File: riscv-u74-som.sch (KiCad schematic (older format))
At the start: 0 parts

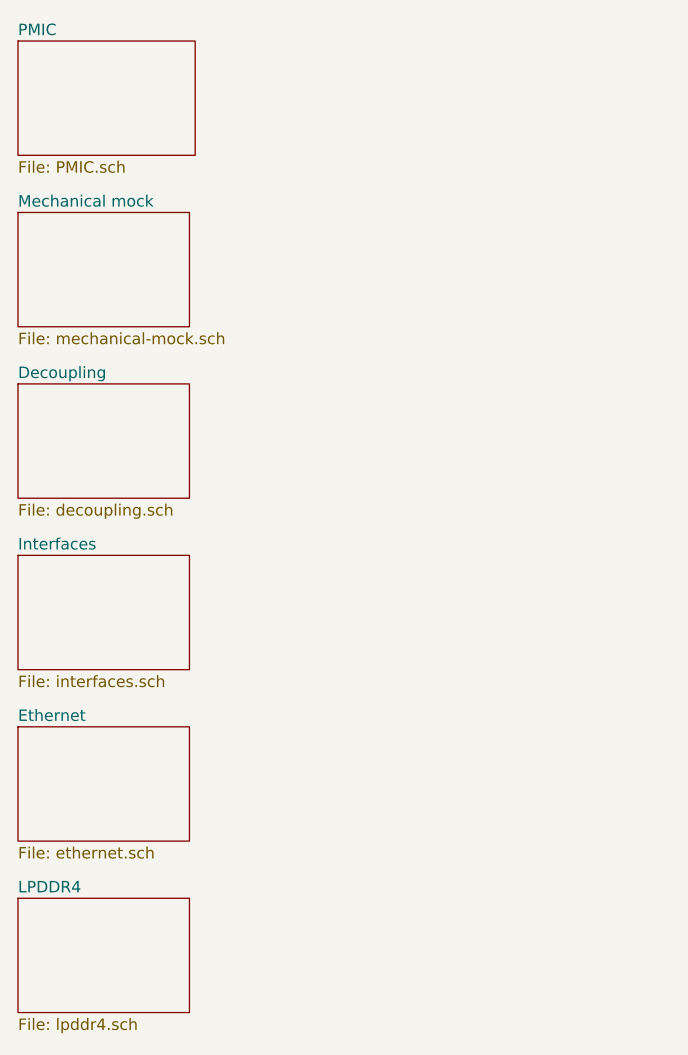
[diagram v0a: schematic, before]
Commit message: Added processor and B2B sheets
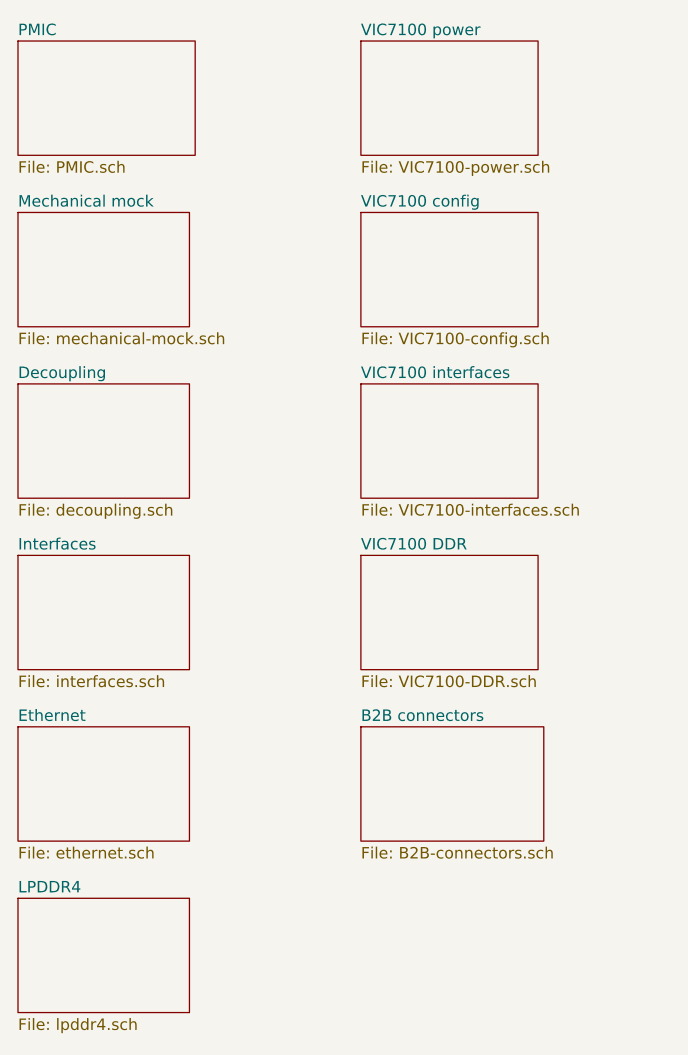
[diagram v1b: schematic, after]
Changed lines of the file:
@@
 $Descr A4 11693 8268
 encoding utf-8
-Sheet 1 7
+Sheet 1 12
 Title ""
 Date ""
@@
 F1 "lpddr4.sch" 50
 $EndSheet
+$Sheet
+S 3000 1000 775  500
+U 60805C73
+F0 "VIC7100 power" 50
+F1 "VIC7100-power.sch" 50
+$EndSheet
+$Sheet
+S 3000 1750 775  500
+U 60805CC6
+F0 "VIC7100 config" 50
+F1 "VIC7100-config.sch" 50
+$EndSheet
+$Sheet
+S 3000 2500 775  500
+U 60805CEC
+F0 "VIC7100 interfaces" 50
+F1 "VIC7100-interfaces.sch" 50
+$EndSheet
+$Sheet
+S 3000 3250 775  500
+U 613A40EE
+F0 "VIC7100 DDR" 50
+F1 "VIC7100-DDR.sch" 50
+$EndSheet
+$Sheet
+S 3000 4000 800  500
+U 6293247C
+F0 "B2B connectors" 50
+F1 "B2B-connectors.sch" 50
+$EndSheet
 $EndSCHEMATC

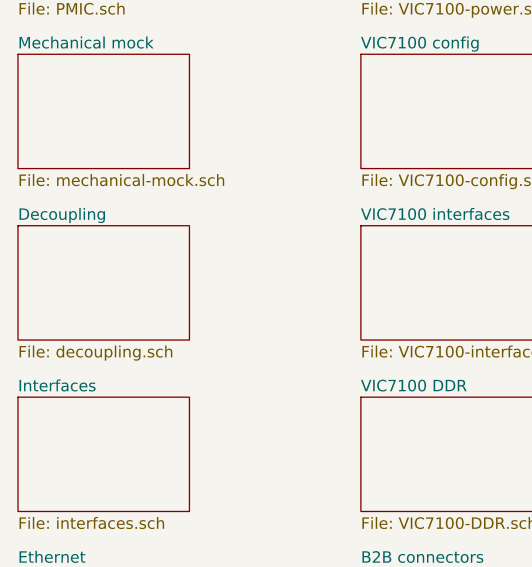
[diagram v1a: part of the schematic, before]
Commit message: Connected interfaces to VIC to visualise its ball locations (wip, mock purposes)
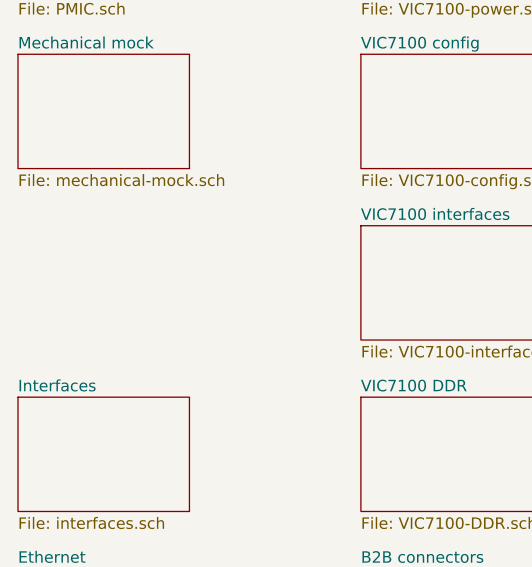
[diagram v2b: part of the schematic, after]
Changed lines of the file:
@@
 $Descr A4 11693 8268
 encoding utf-8
-Sheet 1 12
+Sheet 1 11
 Title ""
 Date ""
@@
 $EndSheet
 $Sheet
-S 1500 2500 750  500
-U 607683D6
-F0 "Decoupling" 50
-F1 "decoupling.sch" 50
-$EndSheet
-$Sheet
